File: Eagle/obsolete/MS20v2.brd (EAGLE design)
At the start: 56 x 100 mm, 62 parts, among them IC1 LM13700M, IC2 TL074D, T1 2N3906, T2 2N3906

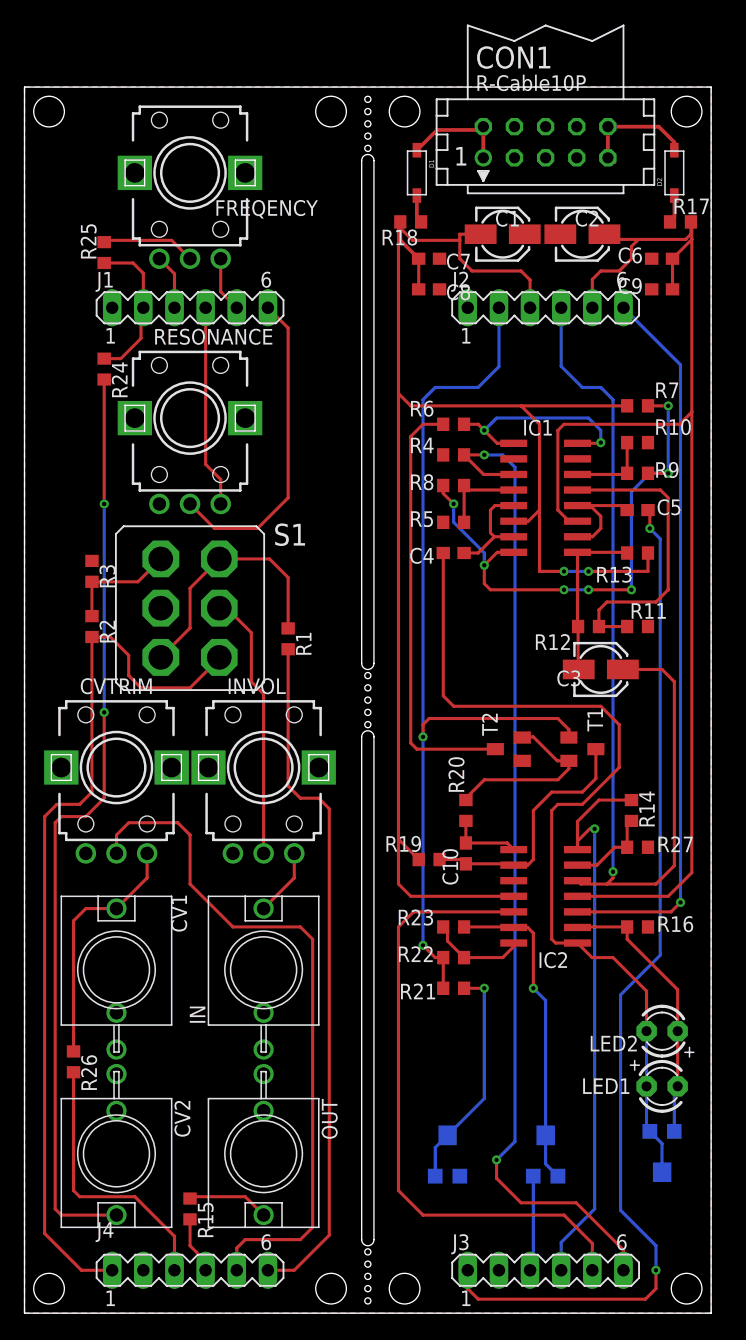
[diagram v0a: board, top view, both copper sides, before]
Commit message: updated drawing for readability
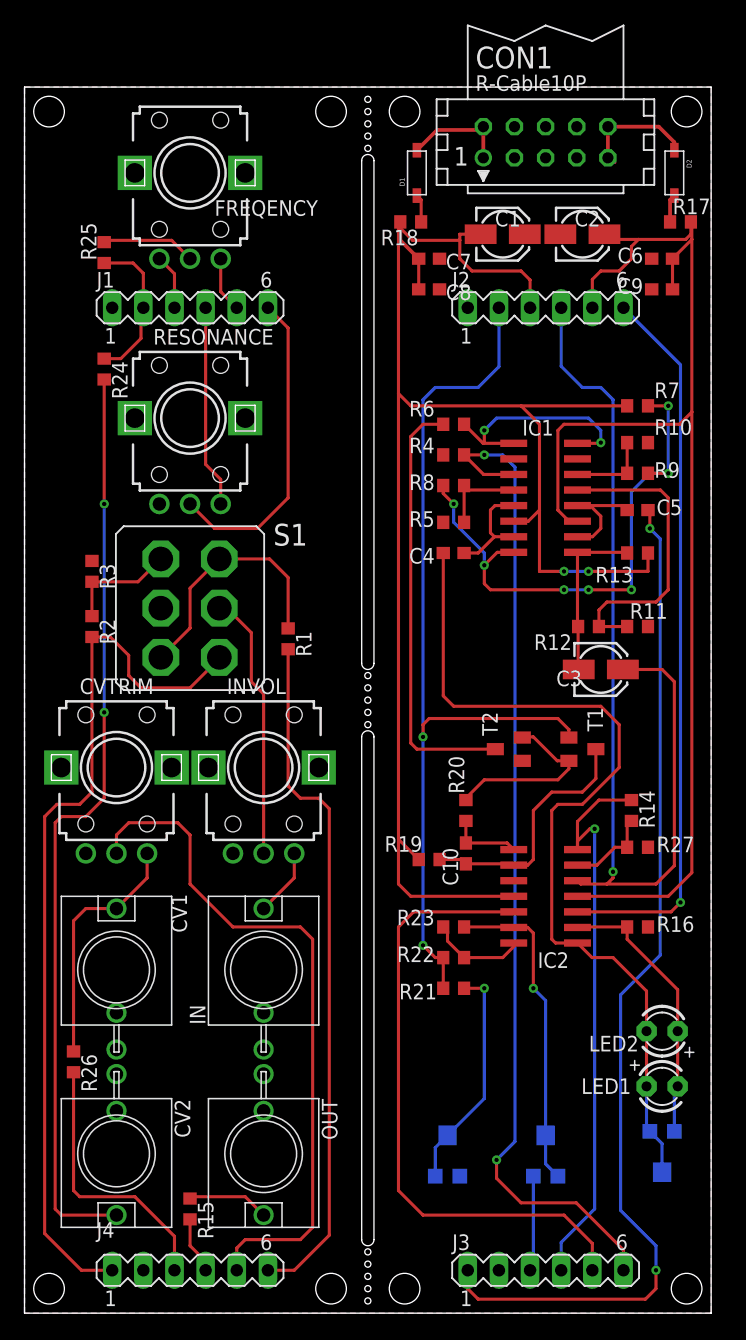
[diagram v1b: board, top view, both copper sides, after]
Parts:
- turned D1 to 90 degrees
- turned D2 to 270 degrees
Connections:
- net N$1: now also D2.C; no longer D2.A
- net N$2: now also D1.A; no longer D1.C
- net N$5: now also D1.C; no longer D1.A
- net N$8: now also D2.A; no longer D2.C
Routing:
- net N$12: track 18.4 -> 19.0 mm
